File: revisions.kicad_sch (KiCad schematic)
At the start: 0 parts

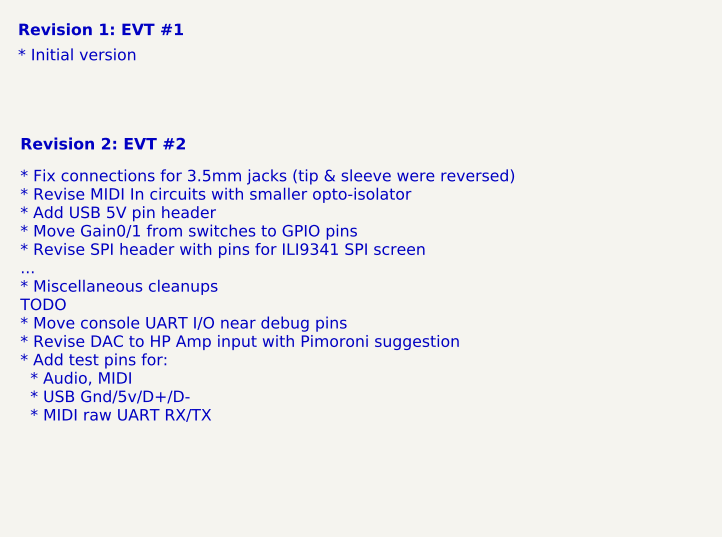
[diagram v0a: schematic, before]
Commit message: Consolidate USART2 Console with SWD debug header
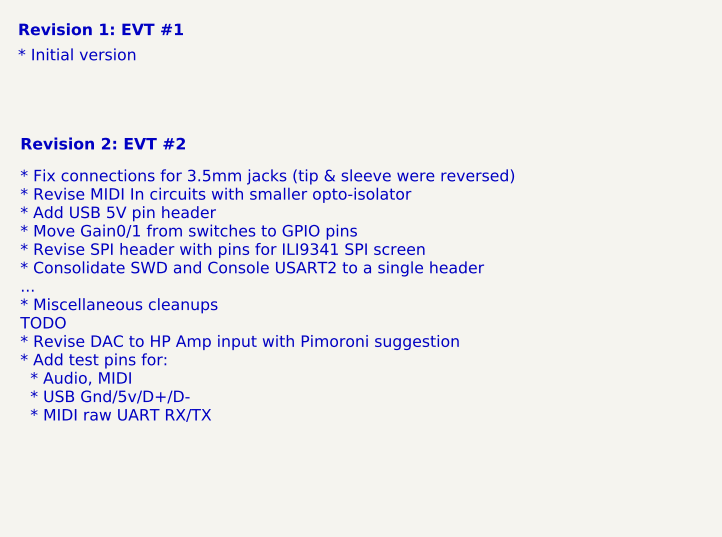
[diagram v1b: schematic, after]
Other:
- note added: "* Fix connections for 3.5mm jacks (tip & sleeve were reversed) * Revise MIDI In circuits with smaller opto-isolator * Add USB 5V pin header * Move Gain0/1 from switches to GPIO pins * Revise SPI header with pins for ILI9341 SPI screen * Consolidate SWD and Console USART2 to a single header ... * Miscellaneous cleanups TODO * Revise DAC to HP Amp input with Pimoroni suggestion * Add test pins for: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"
- note removed: "* Fix connections for 3.5mm jacks (tip & sleeve were reversed) * Revise MIDI In circuits with smaller opto-isolator * Add USB 5V pin header * Move Gain0/1 from switches to GPIO pins * Revise SPI header with pins for ILI9341 SPI screen ... * Miscellaneous cleanups TODO * Move console UART I/O near debug pins * Revise DAC to HP Amp input with Pimoroni suggestion * Add test pins for: * Audio, MIDI *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"
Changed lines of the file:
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@@
 		)
 	)
-	(text "* Fix connections for 3.5mm jacks (tip & sleeve were reversed)\n* Revise MIDI In circuits with smaller opto-isolator\n* Add USB 5V pin header\n* Move Gain0/1 from switches to GPIO pins\n* Revise SPI header with pins for ILI9341 SPI screen\n...\n* Miscellaneous cleanups\nTODO\n* Move console UART I/O near debug pins\n* Revise DAC to HP Amp input with Pimoroni suggestion\n* Add test pins for:\n  * Audio, MIDI\n  * USB Gnd/5v/D+/D-\n  * MIDI raw UART RX/TX\n"
+	(text "* Fix connections for 3.5mm jacks (tip & sleeve were reversed)\n* Revise MIDI In circuits with smaller opto-isolator\n* Add USB 5V pin header\n* Move Gain0/1 from switches to GPIO pins\n* Revise SPI header with pins for ILI9341 SPI screen\n* Consolidate SWD and Console USART2 to a single header\n...\n* Miscellaneous cleanups\nTODO\n* Revise DAC to HP Amp input with Pimoroni suggestion\n* Add test pins for:\n  * Audio, MIDI\n  * USB Gnd/5v/D+/D-\n  * MIDI raw UART RX/TX\n"
 		(exclude_from_sim no)
 		(at 25.4 42.418 0)

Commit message: Consolidate UART5 with 4 & 6 on a single header
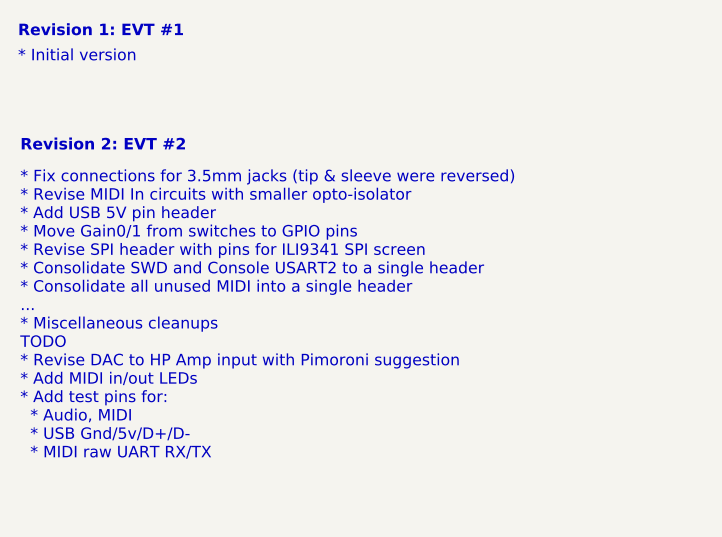
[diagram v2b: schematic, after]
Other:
- note added: "* Fix connections for 3.5mm jacks (tip & sleeve were reversed) * Revise MIDI In circuits with smaller opto-isolator * Add USB 5V pin header * Move Gain0/1 from switches to GPIO pins * Revise SPI header with pins for ILI9341 SPI screen * Consolidate SWD and Console USART2 to a single header * Consolidate all unused MIDI into a single header ... * Miscellaneous cleanups TODO * Revise DAC to HP Amp 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"
- note removed: "* Fix connections for 3.5mm jacks (tip & sleeve were reversed) * Revise MIDI In circuits with smaller opto-isolator * Add USB 5V pin header * Move Gain0/1 from switches to GPIO pins * Revise SPI header with pins for ILI9341 SPI screen * Consolidate SWD and Console USART2 to a single header ... * Miscellaneous cleanups TODO * Revise DAC to HP Amp input with Pimoroni suggestion * Add test pins for: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"
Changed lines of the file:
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@@
 		)
 	)
-	(text "* Fix connections for 3.5mm jacks (tip & sleeve were reversed)\n* Revise MIDI In circuits with smaller opto-isolator\n* Add USB 5V pin header\n* Move Gain0/1 from switches to GPIO pins\n* Revise SPI header with pins for ILI9341 SPI screen\n* Consolidate SWD and Console USART2 to a single header\n...\n* Miscellaneous cleanups\nTODO\n* Revise DAC to HP Amp input with Pimoroni suggestion\n* Add test pins for:\n  * Audio, MIDI\n  * USB Gnd/5v/D+/D-\n  * MIDI raw UART RX/TX\n"
+	(text "* Fix connections for 3.5mm jacks (tip & sleeve were reversed)\n* Revise MIDI In circuits with smaller opto-isolator\n* Add USB 5V pin header\n* Move Gain0/1 from switches to GPIO pins\n* Revise SPI header with pins for ILI9341 SPI screen\n* Consolidate SWD and Console USART2 to a single header\n* Consolidate all unused MIDI into a single header\n...\n* Miscellaneous cleanups\nTODO\n* Revise DAC to HP Amp input with Pimoroni suggestion\n* Add MIDI in/out LEDs\n* Add test pins for:\n  * Audio, MIDI\n  * USB Gnd/5v/D+/D-\n  * MIDI raw UART RX/TX\n"
 		(exclude_from_sim no)
 		(at 25.4 42.418 0)

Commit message: Add female jumper to allow experimenting with Pimoroni circuit (default 1kΩ). Minor cleanups.
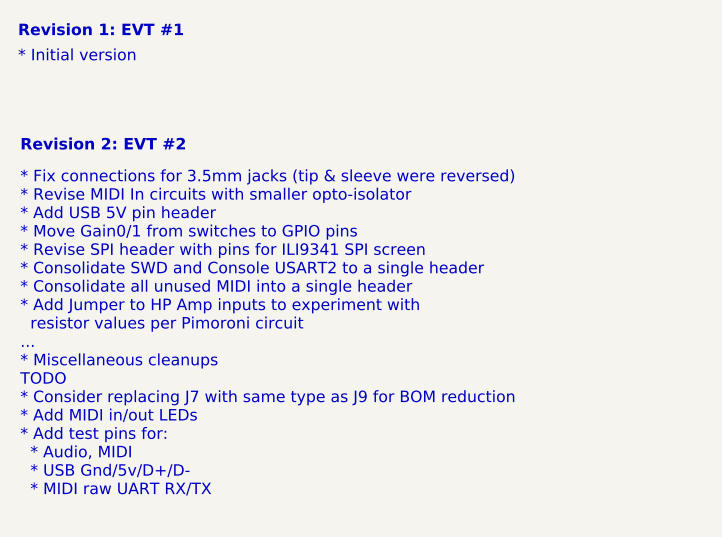
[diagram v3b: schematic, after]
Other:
- note added: "* Fix connections for 3.5mm jacks (tip & sleeve were reversed) * Revise MIDI In circuits with smaller opto-isolator * Add USB 5V pin header * Move Gain0/1 from switches to GPIO pins * Revise SPI header with pins for ILI9341 SPI screen * Consolidate SWD and Console USART2 to a single header * Consolidate all unused MIDI into a single header * Add Jumper to HP Amp inputs to experiment with resistor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"
- note removed: "* Fix connections for 3.5mm jacks (tip & sleeve were reversed) * Revise MIDI In circuits with smaller opto-isolator * Add USB 5V pin header * Move Gain0/1 from switches to GPIO pins * Revise SPI header with pins for ILI9341 SPI screen * Consolidate SWD and Console USART2 to a single header * Consolidate all unused MIDI into a single header ... * Miscellaneous cleanups TODO * Revise DAC to HP Amp 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"
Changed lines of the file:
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@@
 		)
 	)
-	(text "* Fix connections for 3.5mm jacks (tip & sleeve were reversed)\n* Revise MIDI In circuits with smaller opto-isolator\n* Add USB 5V pin header\n* Move Gain0/1 from switches to GPIO pins\n* Revise SPI header with pins for ILI9341 SPI screen\n* Consolidate SWD and Console USART2 to a single header\n* Consolidate all unused MIDI into a single header\n...\n* Miscellaneous cleanups\nTODO\n* Revise DAC to HP Amp input with Pimoroni suggestion\n* Add MIDI in/out LEDs\n* Add test pins for:\n  * Audio, MIDI\n  * USB Gnd/5v/D+/D-\n  * MIDI raw UART RX/TX\n"
+	(text "* Fix connections for 3.5mm jacks (tip & sleeve were reversed)\n* Revise MIDI In circuits with smaller opto-isolator\n* Add USB 5V pin header\n* Move Gain0/1 from switches to GPIO pins\n* Revise SPI header with pins for ILI9341 SPI screen\n* Consolidate SWD and Console USART2 to a single header\n* Consolidate all unused MIDI into a single header\n* Add Jumper to HP Amp inputs to experiment with\n  resistor values per Pimoroni circuit\n...\n* Miscellaneous cleanups\nTODO\n* Consider replacing J7 with same type as J9 for BOM reduction\n* Add MIDI in/out LEDs\n* Add test pins for:\n  * Audio, MIDI\n  * USB Gnd/5v/D+/D-\n  * MIDI raw UART RX/TX\n"
 		(exclude_from_sim no)
 		(at 25.4 42.418 0)

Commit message: Received EVT #2 boards. Testing so far reveals no problems.
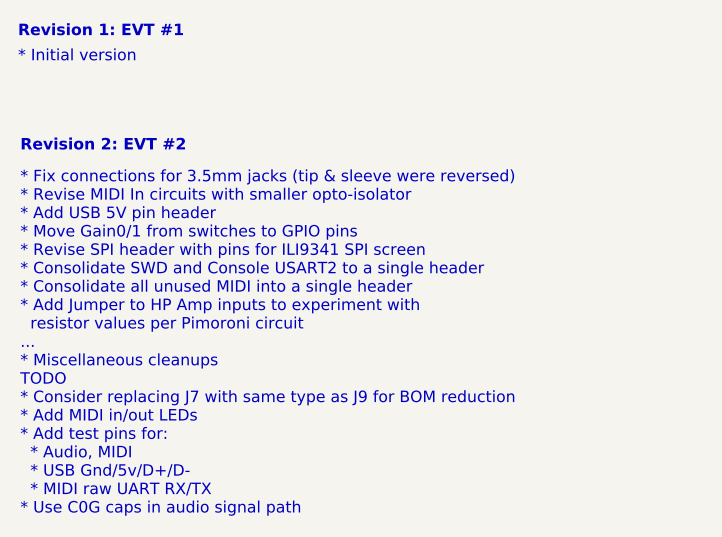
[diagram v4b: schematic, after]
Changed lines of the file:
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@@
 		)
 	)
-	(text "* Fix connections for 3.5mm jacks (tip & sleeve were reversed)\n* Revise MIDI In circuits with smaller opto-isolator\n* Add USB 5V pin header\n* Move Gain0/1 from switches to GPIO pins\n* Revise SPI header with pins for ILI9341 SPI screen\n* Consolidate SWD and Console USART2 to a single header\n* Consolidate all unused MIDI into a single header\n* Add Jumper to HP Amp inputs to experiment with\n  resistor values per Pimoroni circuit\n...\n* Miscellaneous cleanups\nTODO\n* Consider replacing J7 with same type as J9 for BOM reduction\n* Add MIDI in/out LEDs\n* Add test pins for:\n  * Audio, MIDI\n  * USB Gnd/5v/D+/D-\n  * MIDI raw UART RX/TX\n"
+	(text "* Fix connections for 3.5mm jacks (tip & sleeve were reversed)\n* Revise MIDI In circuits with smaller opto-isolator\n* Add USB 5V pin header\n* Move Gain0/1 from switches to GPIO pins\n* Revise SPI header with pins for ILI9341 SPI screen\n* Consolidate SWD and Console USART2 to a single header\n* Consolidate all unused MIDI into a single header\n* Add Jumper to HP Amp inputs to experiment with\n  resistor values per Pimoroni circuit\n...\n* Miscellaneous cleanups\nTODO\n* Consider replacing J7 with same type as J9 for BOM reduction\n* Add MIDI in/out LEDs\n* Add test pins for:\n  * Audio, MIDI\n  * USB Gnd/5v/D+/D-\n  * MIDI raw UART RX/TX\n* Use C0G caps in audio signal path\n"
 		(exclude_from_sim no)
 		(at 25.4 42.418 0)
